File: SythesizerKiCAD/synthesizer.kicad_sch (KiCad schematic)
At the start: 41 parts, among them U2 LM1877, U3 LM324A

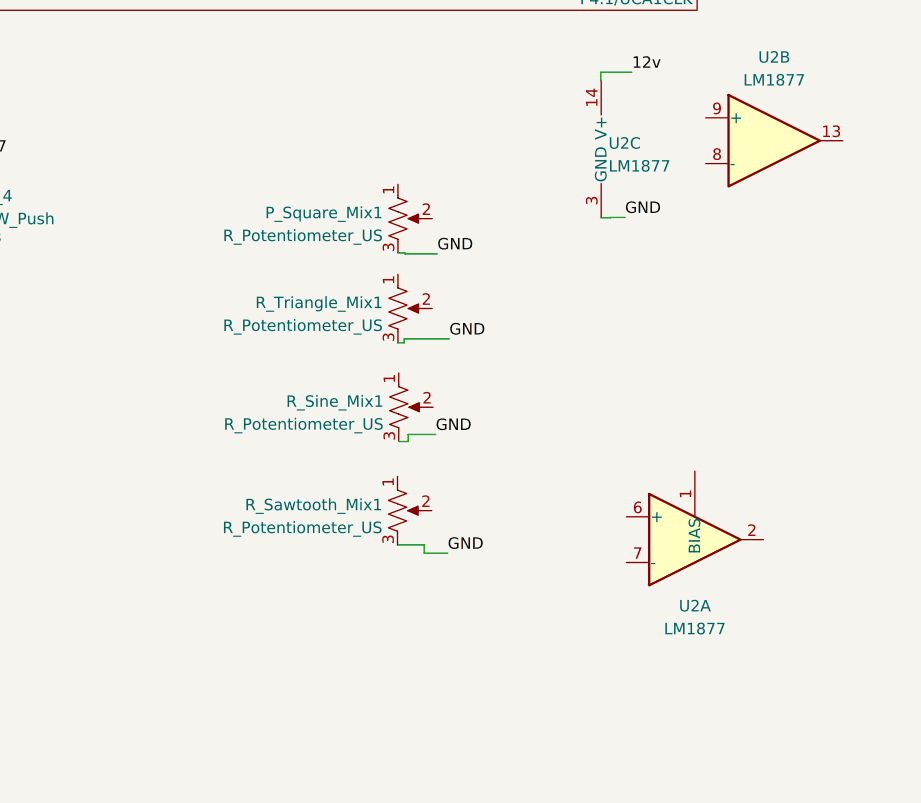
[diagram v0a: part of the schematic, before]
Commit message: Lowpass filters and isolators
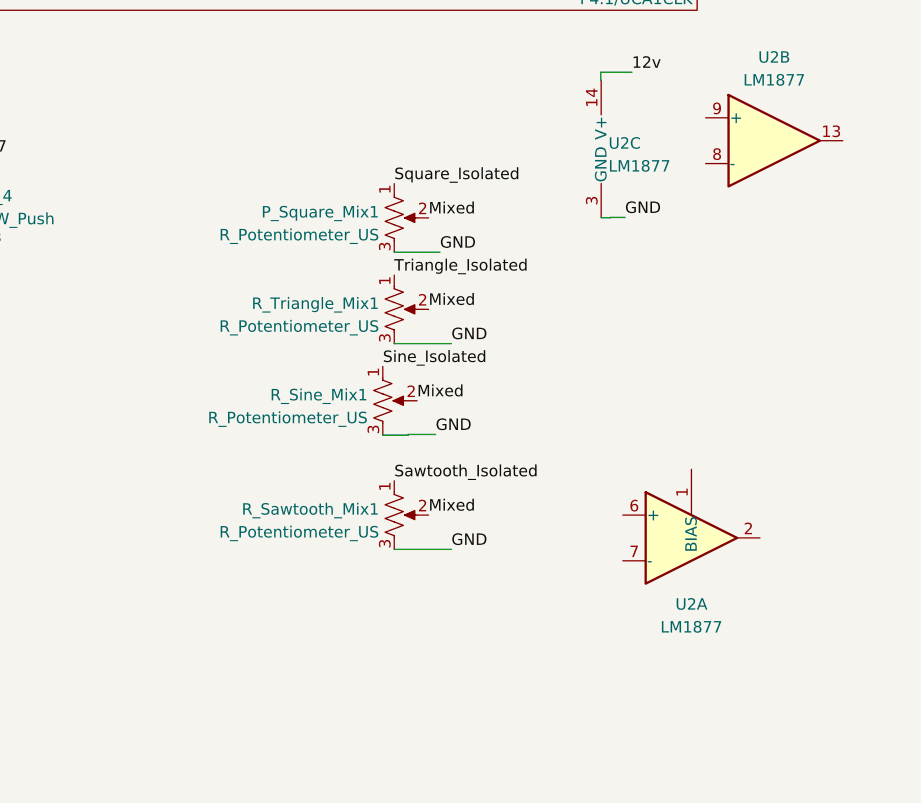
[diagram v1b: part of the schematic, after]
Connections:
- net Sawtooth_Isolated: now also R_Sawtooth_Mix1.1
- net Sine_Isolated: now also R_Sine_Mix1.1
- net Square_Isolated: now also P_Square_Mix1.1
- net Triangle_Isolated: now also R_Triangle_Mix1.1
- net Mixed: now reaches R_Triangle_Mix1.2
- net Mixed: now also P_Square_Mix1.2, R_Sawtooth_Mix1.2, R_Sine_Mix1.2
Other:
- moved on the sheet: R_Sawtooth_Mix1, R_Sine_Mix1

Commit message: Volume, audio out, power in
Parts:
- removed U3: LM324A, Package_DIP:DIP-14_W7.62mm, symbol Amplifier_Operational:LM324A
- added 3v3, 9v1, Audio_Out1, GND1, GND2: Conn_01x01_Pin, Connector_Wire:SolderWire-0.1sqmm_1x01_D0.4mm_OD1mm, symbol Connector:Conn_01x01_Pin
- added R1, R4, R6, R8, R9: 100k, Resistor_THT:R_Axial_DIN0207_L6.3mm_D2.5mm_P2.54mm_Vertical, symbol Device:R_US
- added R2, R3, R5, R7: 300k, Resistor_THT:R_Axial_DIN0207_L6.3mm_D2.5mm_P2.54mm_Vertical, symbol Device:R_US
- added R_Volume1: R_Potentiometer_US, Potentiometer_THT:Potentiometer_Alpha_RD901F-40-00D_Single_Vertical, symbol Device:R_Potentiometer_US
- added U3: LMC6484, Package_DIP:DIP-14_W7.62mm, symbol Amplifier_Operational:LMC6484
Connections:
- net 3v3: now also 3v3.1 (Pin_1), U3.4 (V+)
- net GND: now also GND1.1 (Pin_1), GND2.1 (Pin_1), R1.2, R4.2, R6.2, R8.2, R9.2, U3.11 (V-)
- net Mixed: now also U2.6 (+)
- net Sawtooth_Analog: now also U3.3 (+)
- net Sawtooth_Isolated: now also R7.1, U3.1, U3.2 (-); no longer R_Sawtooth_Mix1.1
- net Sine_Analog: now also U3.12 (+)
- net Sine_Isolated: now also R3.1, U3.13 (-), U3.14; no longer R_Sine_Mix1.1
- net Square_Analog: now also U3.10 (+)
- net Square_Isolated: now also R2.1, U3.8, U3.9 (-); no longer P_Square_Mix1.1
- net Triangle_Analog: now also U3.5 (+)
- net Triangle_Isolated: now also R5.1, U3.6 (-), U3.7; no longer R_Triangle_Mix1.1
- net Audio_Out: now reaches U2.2
- net Audio_Out: now also Audio_Out1.1 (Pin_1), R_Volume1.2
- net at U2.7 (-): now also R9.1, R_Volume1.1
- net 12v renamed 9v
- net 9v: now also 9v1.1 (Pin_1)
- new net Sawtooth_Divided: R7.2, R8.1, R_Sawtooth_Mix1.1
- new net Sine_Divided: R3.2, R4.1, R_Sine_Mix1.1
- new net Square_Divided: P_Square_Mix1.1, R1.1, R2.2
- new net Triangle_Divided: R5.2, R6.1, R_Triangle_Mix1.1
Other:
- moved on the sheet: U2A
